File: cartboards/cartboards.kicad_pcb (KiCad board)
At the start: 4 copper layers, 152.4 x 58.4 mm, 7 parts, among them J1 CES-106-01-T-S, J2 CES-106-01-T-S, J3 CES-106-01-T-S, J4 CES-106-01-T-S, J5 CES-132-02-T-S, J6 CES-132-02-T-S

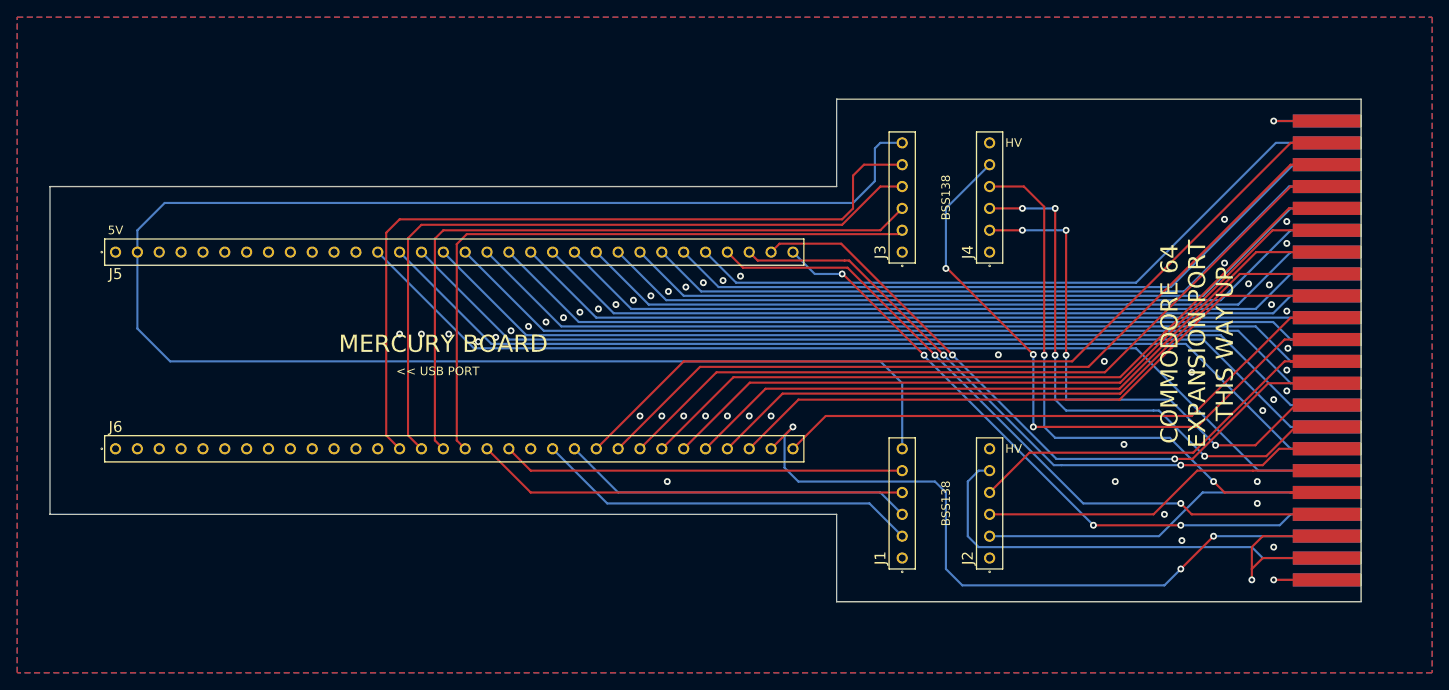
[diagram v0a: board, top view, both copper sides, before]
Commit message: Tweak trace width for power in schematics
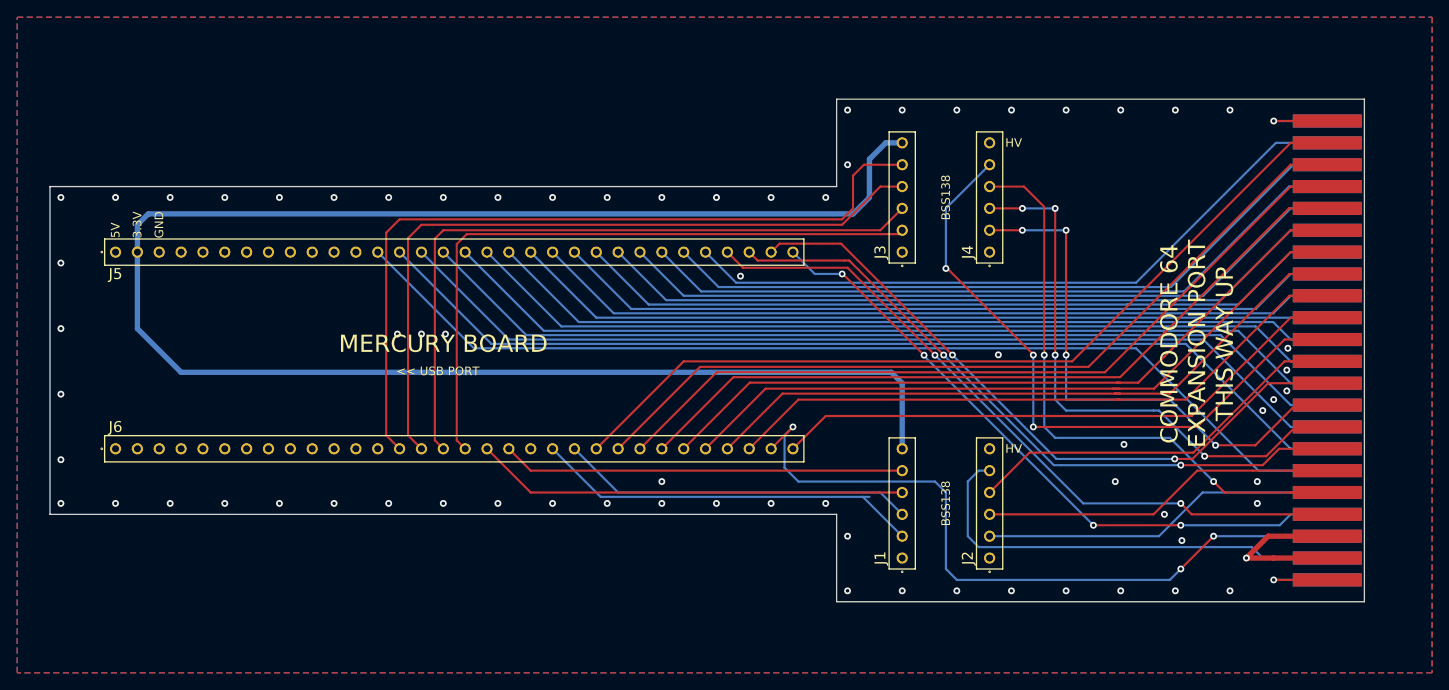
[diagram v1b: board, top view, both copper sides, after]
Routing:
- net C64_2_5V: track 26.1 -> 23.5 mm
- net /CLK0: track 44.8 -> 45.6 mm
- net +3V3: track 205.9 -> 206.7 mm
- net /DATA6: track 78.1 -> 78.8 mm
- net C64_C_RESET: track 85.1 -> 84.5 mm
- net /DATA5: track 82.0 -> 82.5 mm
- net C64_1_GND: vias 52 -> 71
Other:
- board size 152.4 x 58.4 mm -> 152.8 x 58.4 mm
- net class Ground added: clearance 0.2, trace_width 0.625, via_dia 0.8, via_drill 0.4
- net class Power added: clearance 0.2, trace_width 0.625, via_dia 0.8, via_drill 0.4
- board text added: "3.3V"
- board text added: "GND"
